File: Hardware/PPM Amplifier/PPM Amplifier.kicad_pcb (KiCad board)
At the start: 2 copper layers, 135.5 x 59.5 mm, 34 parts, among them J1 Power In, J2 Signal In, J3 TP1, J4 TP2, J5 TP3, P2 Signal Out, SW1 SW_DIP_x12, T1 42TL016, U3 OP177G

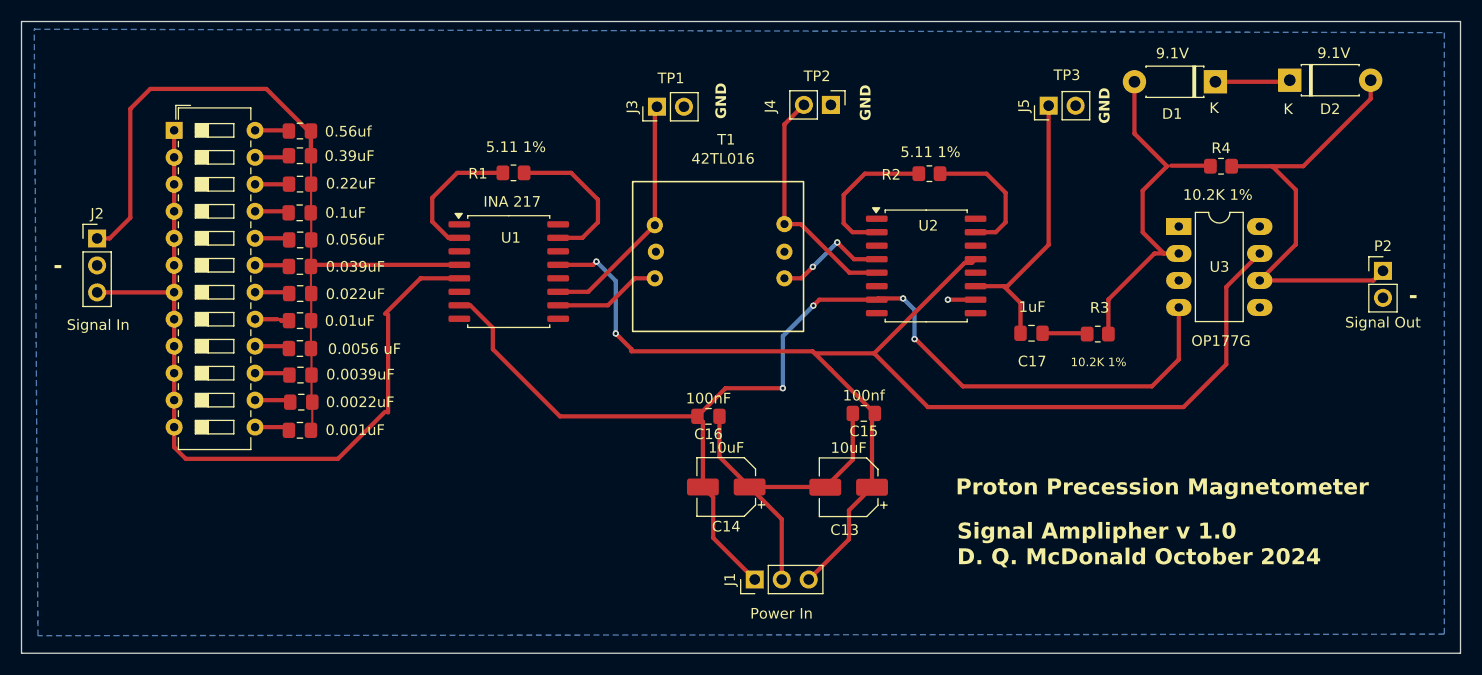
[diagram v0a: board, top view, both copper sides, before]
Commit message: Update on Amp Layout
Added power LED
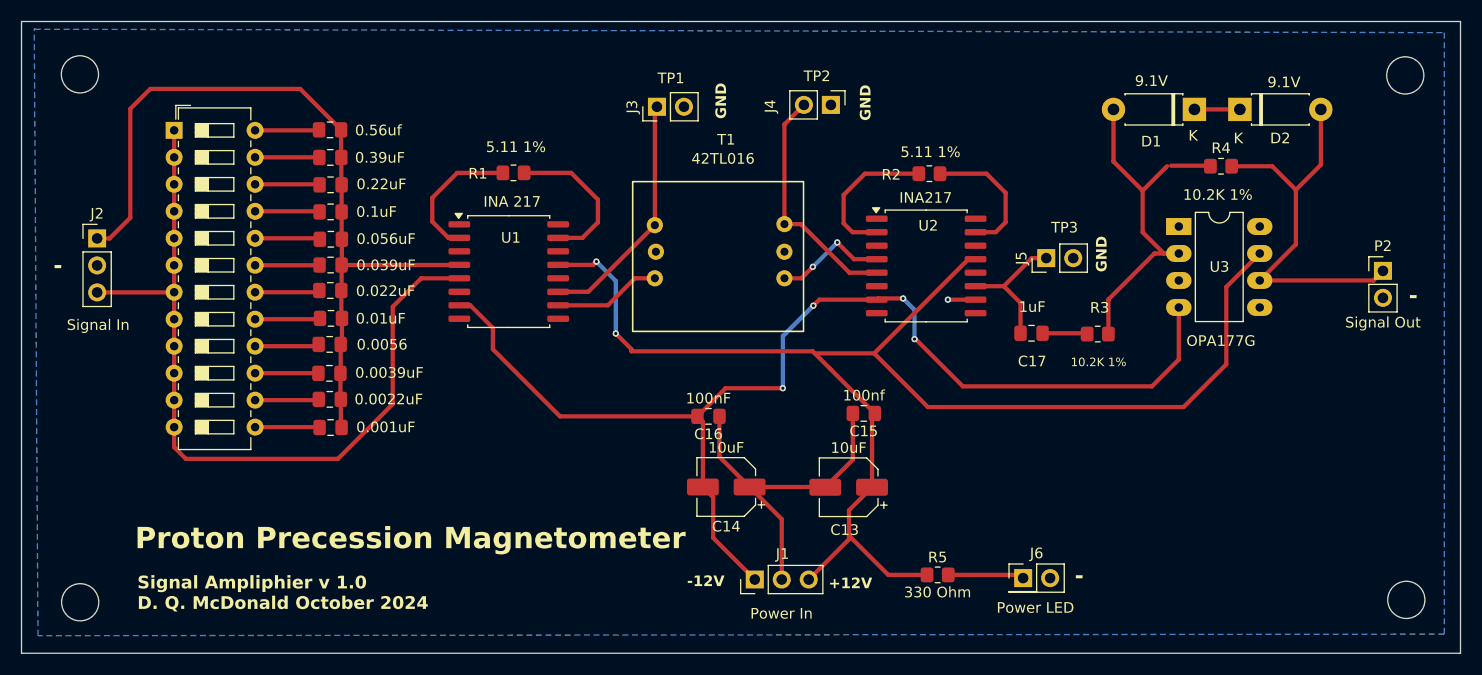
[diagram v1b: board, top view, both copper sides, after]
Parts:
- added J6: Power LED, Connector_PinHeader_2.54mm:PinHeader_2x01_P2.54mm_Vertical, F.Cu at (119.5, 71.5)
- added R5: 330 Ohm, Resistor_SMD:R_0805_2012Metric_Pad1.20x1.40mm_HandSolder, F.Cu at (111.5, 71.2)
- added REF**: MountingHole_3.5mm, MountingHole:MountingHole_3.5mm, F.Cu at (155.5, 24.1)
- added REF**: MountingHole_3.5mm, MountingHole:MountingHole_3.5mm, F.Cu at (30.7, 73.8)
- added REF**: MountingHole_3.5mm, MountingHole:MountingHole_3.5mm, F.Cu at (30.7, 24.1)
- added REF**: MountingHole_3.5mm, MountingHole:MountingHole_3.5mm, F.Cu at (155.6, 73.5)
- C9: value 0.0056 uF -> 0.0056
- U3: value OP177G -> OPA177G
- moved J5 14.4 mm to (121.7, 41.4)
- moved D2 5.44 mm to (139.9, 27.4)
- moved D1 3.27 mm to (135.6, 27.4)
- moved C8 2.92 mm to (54.3, 47.0)
- moved C4 2.91 mm to (54.3, 37.0)
- moved C12 2.90 mm to (54.3, 57.3)
- moved C6 2.89 mm to (54.3, 42.0)
- moved C5 2.89 mm to (54.3, 39.6)
- moved C3 2.88 mm to (54.3, 34.5)
- moved C2 2.87 mm to (54.3, 31.9)
- moved C7 2.85 mm to (54.3, 44.4)
- moved C1 2.84 mm to (54.2, 29.3)
- moved C9 2.83 mm to (54.2, 49.5)
- moved C10 2.73 mm to (54.2, 52.2)
- moved C11 2.70 mm to (54.2, 54.6)
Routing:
- net Net-(J5-Pin_1): track 26.7 -> 12.8 mm
- net +12V: track 124.6 -> 132.7 mm
- net Net-(J6-Pin_1): track 0.00 -> 7.17 mm
- net Net-(D2-A): track 42.5 -> 37.4 mm
- net Net-(C12-Pad1): track 2.99 -> 6.43 mm
- net Net-(C9-Pad1): track 2.96 -> 6.29 mm
- net Net-(C11-Pad1): track 3.07 -> 6.36 mm
- net Net-(C10-Pad1): track 2.99 -> 6.26 mm
- net Net-(C5-Pad1): track 2.95 -> 6.19 mm
- net Net-(C4-Pad1): track 2.90 -> 6.12 mm
- net Net-(C7-Pad1): track 2.94 -> 6.14 mm
- net Net-(C6-Pad1): track 2.91 -> 6.09 mm
- net Net-(C3-Pad1): track 2.94 -> 6.09 mm
- net Net-(C2-Pad1): track 2.98 -> 6.13 mm
- net Net-(C1-Pad1): track 2.89 -> 6.04 mm
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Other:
- board text added: "+12V"
- board text added: "-12V"
- board text added: "Signal Ampliphier v 1.0 D. Q. McDonald October 2024"
- board text removed: "Signal Amplipher v 1.0 D. Q. McDonald October 2024"

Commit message: Final version of AMP
Sent to manufacture
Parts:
- SW1: footprint Button_Switch_THT:SW_DIP_SPSTx12_Slide_6.7x32.04mm_W7.62mm_P2.54mm_LowProfile -> Button_Switch_SMD:SW_DIP_SPSTx12_Slide_6.7x32.04mm_W8.61mm_P2.54mm_LowProfile
- U3: value OPA177G -> OP177G
- moved SW1 14.6 mm to (43.9, 43.3)
